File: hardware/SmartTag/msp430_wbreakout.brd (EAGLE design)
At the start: 33 x 40.6 mm, 21 parts, among them U1 ADXL362

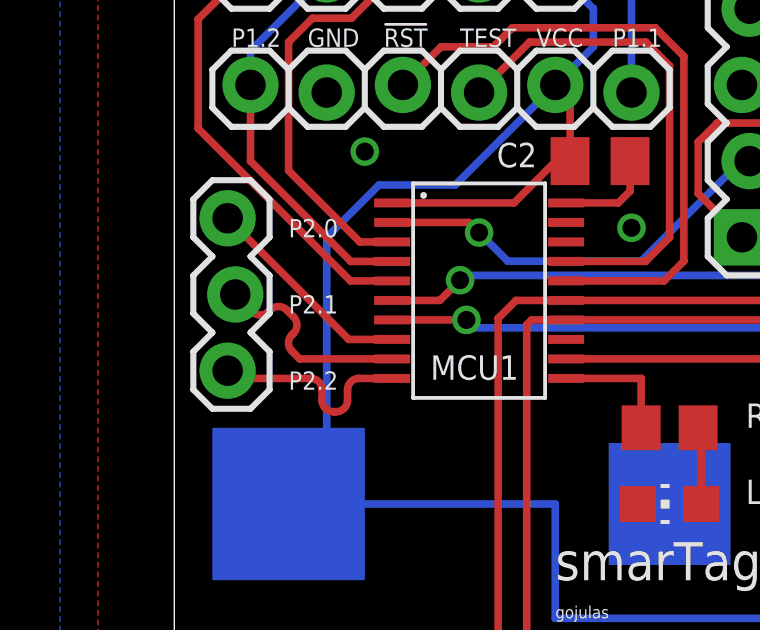
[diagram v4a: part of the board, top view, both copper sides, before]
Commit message: hw: Rework capacitive sensor traces
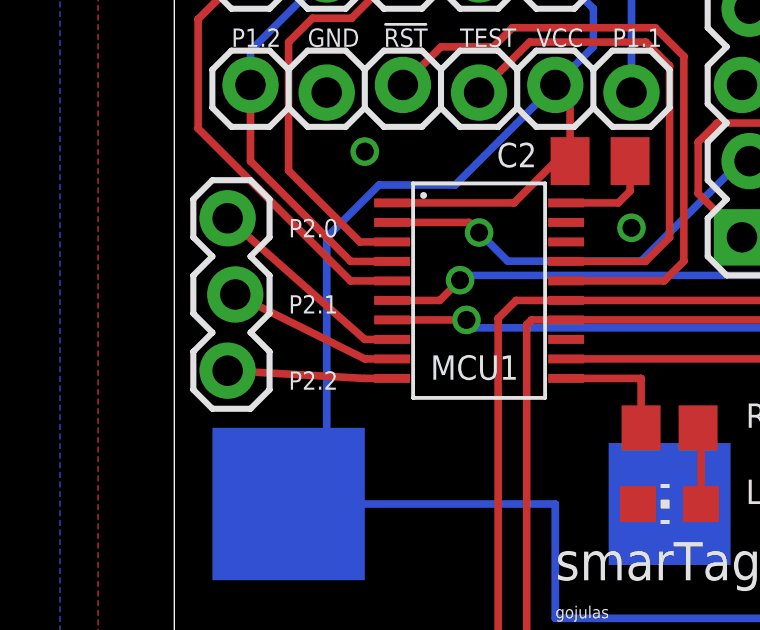
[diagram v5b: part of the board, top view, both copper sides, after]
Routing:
- net P2.2_C: track 6.92 -> 5.49 mm
- net P2.1_C: track 6.92 -> 5.73 mm
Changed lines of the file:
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@@
 <setting verticaltext="up"/>
 </settings>
-<grid distance="0.05" unitdist="inch" unit="inch" style="lines" multiple="1" display="yes" altdistance="0.00625" altunitdist="inch" altunit="inch"/>
+<grid distance="0.05" unitdist="inch" unit="inch" style="lines" multiple="1" display="yes" altdistance="0.000000123031" altunitdist="inch" altunit="inch"/>
 <layers>
 <layer number="1" name="Top" color="4" fill="1" visible="yes" active="yes"/>
@@
 <contactref element="MCU1" pad="8"/>
 <contactref element="JP8" pad="3"/>
-<wire x1="7.2599" y1="25.807" x2="5.816" y2="25.807" width="0.254" layer="1"/>
-<wire x1="5.816" y1="25.807" x2="1.778" y2="29.845" width="0.254" layer="1"/>
+<wire x1="7.2599" y1="25.807" x2="6.35" y2="25.807" width="0.254" layer="1"/>
+<wire x1="6.35" y1="25.807" x2="1.778" y2="29.845" width="0.254" layer="1"/>
 </signal>
 <signal name="P2.1_C" class="1">
 <contactref element="MCU1" pad="9"/>
 <contactref element="JP8" pad="2"/>
-<wire x1="7.2599" y1="25.157" x2="4.18" y2="25.157" width="0.254" layer="1"/>
-<wire x1="4.18" y1="25.157" x2="3.91713125" y2="25.41986875" width="0.254" layer="1"/>
-<wire x1="3.91713125" y1="25.41986875" x2="3.91713125" y2="25.958684375" width="0.254" layer="1" curve="-90"/>
-<wire x1="3.91713125" y1="25.958684375" x2="3.9761625" y2="26.017715625" width="0.254" layer="1"/>
-<wire x1="3.9761625" y1="26.017715625" x2="3.9761625" y2="26.556534375" width="0.254" layer="1" curve="90"/>
-<wire x1="3.9761625" y1="26.556534375" x2="3.740165625" y2="26.79253125" width="0.254" layer="1"/>
-<wire x1="3.740165625" y1="26.79253125" x2="3.201346875" y2="26.79253125" width="0.254" layer="1" curve="90"/>
-<wire x1="3.201346875" y1="26.79253125" x2="3.142315625" y2="26.7335" width="0.254" layer="1"/>
-<wire x1="3.142315625" y1="26.7335" x2="2.6035" y2="26.7335" width="0.254" layer="1" curve="-90"/>
-<wire x1="2.6035" y1="26.7335" x2="2.032" y2="27.305" width="0.254" layer="1"/>
+<wire x1="7.2599" y1="25.157" x2="6.35" y2="25.157" width="0.254" layer="1"/>
+<wire x1="6.35" y1="25.157" x2="2.032" y2="27.305" width="0.254" layer="1"/>
 </signal>
 <signal name="P2.2_C" class="1">
 <contactref element="MCU1" pad="10"/>
 <contactref element="JP8" pad="1"/>
-<wire x1="7.2599" y1="24.5071" x2="6.15530625" y2="24.5071" width="0.254" layer="1"/>
-<wire x1="6.15530625" y1="24.5071" x2="5.77430625" y2="24.1261" width="0.254" layer="1" curve="90"/>
-<wire x1="5.77430625" y1="24.1261" x2="5.77430625" y2="23.7781625" width="0.254" layer="1"/>
-<wire x1="5.77430625" y1="23.7781625" x2="5.39330625" y2="23.3971625" width="0.254" layer="1" curve="-90"/>
-<wire x1="5.39330625" y1="23.3971625" x2="5.306571875" y2="23.3971625" width="0.254" layer="1"/>
-<wire x1="5.306571875" y1="23.3971625" x2="4.925571875" y2="23.7781625" width="0.254" layer="1" curve="-90"/>
-<wire x1="4.925571875" y1="23.7781625" x2="4.925571875" y2="24.1261" width="0.254" layer="1"/>
-<wire x1="4.925571875" y1="24.1261" x2="4.544571875" y2="24.5071" width="0.254" layer="1" curve="90"/>
-<wire x1="2.0359" y1="24.5071" x2="1.778" y2="24.765" width="0.254" layer="1"/>
-<wire x1="4.544571875" y1="24.5071" x2="2.0359" y2="24.5071" width="0.254" layer="1"/>
+<wire x1="7.2599" y1="24.5071" x2="6.35" y2="24.5071" width="0.254" layer="1"/>
+<wire x1="6.35" y1="24.5071" x2="1.778" y2="24.765" width="0.254" layer="1"/>
 </signal>
 <signal name="DVSS">
